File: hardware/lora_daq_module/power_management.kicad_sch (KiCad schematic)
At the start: 28 parts, among them J7 Conn_01x02, U6 MCP1700x-330xxTT, U7 TPS2116DRL, U8 TPS63002, U9 MCP73833

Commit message: assign parts and update BOM in symbol field table, warn: pcb footprints need update
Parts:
- C14: Desc (none) -> CAP CER 0.047UF 25V X7R 0603; Dist (none) -> Digikey; Dist PN (none) -> 311-1373-1-ND; Mfr (none) -> YAGEO; Mfr PN (none) -> CC0603KRX7R8BB473
- C15, C16, C17, C20, C21: Desc (none) -> CAP CER 1UF 16V X7R 0603; Dist (none) -> Digikey; Dist PN (none) -> 490-5241-1-ND; Mfr (none) -> Murata Electronics; Mfr PN (none) -> GCM188R71C105KA64D
- C18: Desc (none) -> CAP CER 10UF 50V X5R 1206; Dist (none) -> Digikey; Dist PN (none) -> 1276-2876-1-ND; Mfr (none) -> Samsung Electro-Mechanics; Mfr PN (none) -> CL31A106KBHNNNE
- C19: footprint Capacitor_SMD:C_1210_3225Metric -> Capacitor_SMD:C_1206_3216Metric; Desc (none) -> CAP CER 33UF 16V JB 1206; Dist (none) -> Digikey; Dist PN (none) -> 445-11694-1-ND; Mfr (none) -> TDK Corporation; Mfr PN (none) -> C3216JB1C336M160AB
- D4: value ~ -> Green; Desc (none) -> Green 571nm LED Indication - Discrete 2V 0603 (1608 Metric); Dist (none) -> Digikey; Dist PN (none) -> 160-1446-1-ND; Mfr (none) -> Lite-On Inc.; Mfr PN (none) -> LTST-C191KGKT
- D5: value ~ -> Yellow; Desc (none) -> Yellow 591nm LED Indication - Discrete 2.1V 0603 (1608 Metr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; Dist (none) -> Digikey; Dist PN (none) -> 160-1448-1-ND; Mfr (none) -> Lite-On Inc.; Mfr PN (none) -> LTST-C191KSKT
- D6: value ~ -> Red; Desc (none) -> Red 631nm LED Indication - Discrete 2V 0603 (1608 Metric); Dist (none) -> Digikey; Dist PN (none) -> 160-1436-1-ND; Mfr (none) -> Lite-On Inc.; Mfr PN (none) -> LTST-C190KRKT
- J7: Desc (none) -> Connector Header Through Hole 2 position 0.100" (2.54mm); Dist (none) -> Digikey; Dist PN (none) -> 732-5315-ND; Mfr (none) -> Würth Elektronik; Mfr PN (none) -> 61300211121
- L2: Desc (none) -> 3.3 µH Shielded Inductor 1.4 A 130mOhm Max Nonstandard; Dist (none) -> Digikey; Dist PN (none) -> 2457-LPS3015-332MRC-ND; Mfr (none) -> Coilcraft; Mfr PN (none) -> LPS3015-332MRC
- R10: Desc (none) -> 680 kOhms ±1% 0.1W, 1/10W Chip Resistor 0603 (1608 Metric) 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; Dist (none) -> Digikey; Dist PN (none) -> 311-680KHRCT-ND; Mfr (none) -> YAGEO; Mfr PN (none) -> RC0603FR-07680KL
- R11: Desc (none) -> 470 kOhms ±1% 0.1W, 1/10W Chip Resistor 0603 (1608 Metric) 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; Dist (none) -> Digikey; Dist PN (none) -> RMCF0603FT470KCT-ND; Mfr (none) -> Stackpole Electronics Inc; Mfr PN (none) -> RMCF0603FT470K
- R12: Desc (none) -> 4.7 kOhms ±5% 0.1W, 1/10W Chip Resistor 0603 (1608 Metric) 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; Dist (none) -> Digikey; Dist PN (none) -> 311-4.7KGRCT-ND; Mfr (none) -> YAGEO; Mfr PN (none) -> RC0603JR-074K7L
- R13, R14, R15: Desc (none) -> 470 Ohms ±5% 0.1W, 1/10W Chip Resistor 0603 (1608 Metric) M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; Dist (none) -> Digikey; Dist PN (none) -> 311-470GRCT-ND; Mfr (none) -> YAGEO; Mfr PN (none) -> RC0603JR-07470RL
- R16, R19: Desc (none) -> 1 kOhms ±1% 0.1W, 1/10W Chip Resistor 0603 (1608 Metric) Au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; Dist (none) -> Digikey; Dist PN (none) -> RMCF0603FT1K00CT-ND; Mfr (none) -> Stackpole Electronics Inc; Mfr PN (none) -> RMCF0603FT1K00
- R17: Desc (none) -> THERMISTOR NTC 10KOHM 3380K 0603; Dist (none) -> Digikey; Dist PN (none) -> 490-16279-1-ND; Mfr (none) -> Murata Electronics; Mfr PN (none) -> NCU18XH103F60RB
- R18: Desc (none) -> 150 kOhms ±1% 0.1W, 1/10W Chip Resistor 0603 (1608 Metric) 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; Dist (none) -> Digikey; Dist PN (none) -> RMCF0603FT150KCT-ND; Mfr (none) -> Stackpole Electronics Inc; Mfr PN (none) -> RMCF0603FT150K
- U6: Desc (none) -> Linear Voltage Regulator IC Positive Fixed 1 Output 250mA S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; Dist (none) -> Digikey; Dist PN (none) -> MCP1700T3302ETTCT-ND; Mfr (none) -> Microchip Technology; Mfr PN (none) -> MCP1700T-3302E/TT
- U7: Desc (none) -> Power Switch/Driver 2:1 N-Channel 2.5A SOT-583; Dist (none) -> Digikey; Dist PN (none) -> 296-TPS2116DRLRCT-ND; Mfr (none) -> Texas Instruments; Mfr PN (none) -> TPS2116DRLR
- U8: Desc (none) -> Buck-Boost Switching Regulator IC Positive Fixed 5V 1 Outpu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; Dist (none) -> Digikey; Dist PN (none) -> 296-19644-1-ND; Mfr (none) -> Texas Instruments; Mfr PN (none) -> TPS63002DRCR
- U9: Desc (none) -> Charger IC Lithium Ion/Polymer 10-MSOP; Dist (none) -> Digikey; Dist PN (none) -> MCP73833T-AMI/UNCT-ND; Mfr (none) -> Microchip Technology; Mfr PN (none) -> MCP73833T-AMI/UN

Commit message: add test points and antenna microstrip
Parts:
- added TP13: tp_batgnd, TestPoint:TestPoint_THTPad_1.5x1.5mm_Drill0.7mm, symbol Connector:TestPoint
- added TP2: tp_vbatt, TestPoint:TestPoint_THTPad_1.5x1.5mm_Drill0.7mm, symbol Connector:TestPoint
- added TP3: tp_5vbatt, TestPoint:TestPoint_THTPad_1.5x1.5mm_Drill0.7mm, symbol Connector:TestPoint
- added TP4: tp_5v, TestPoint:TestPoint_THTPad_1.5x1.5mm_Drill0.7mm, symbol Connector:TestPoint
- added TP5: tp_3v3, TestPoint:TestPoint_THTPad_1.5x1.5mm_Drill0.7mm, symbol Connector:TestPoint
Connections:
- net +3.3V: now also TP5.1
- net +5V: now also TP4.1
- net +5V_bat: now also TP3.1
- net +VBATT: now also TP2.1
- net GND: now also TP13.1

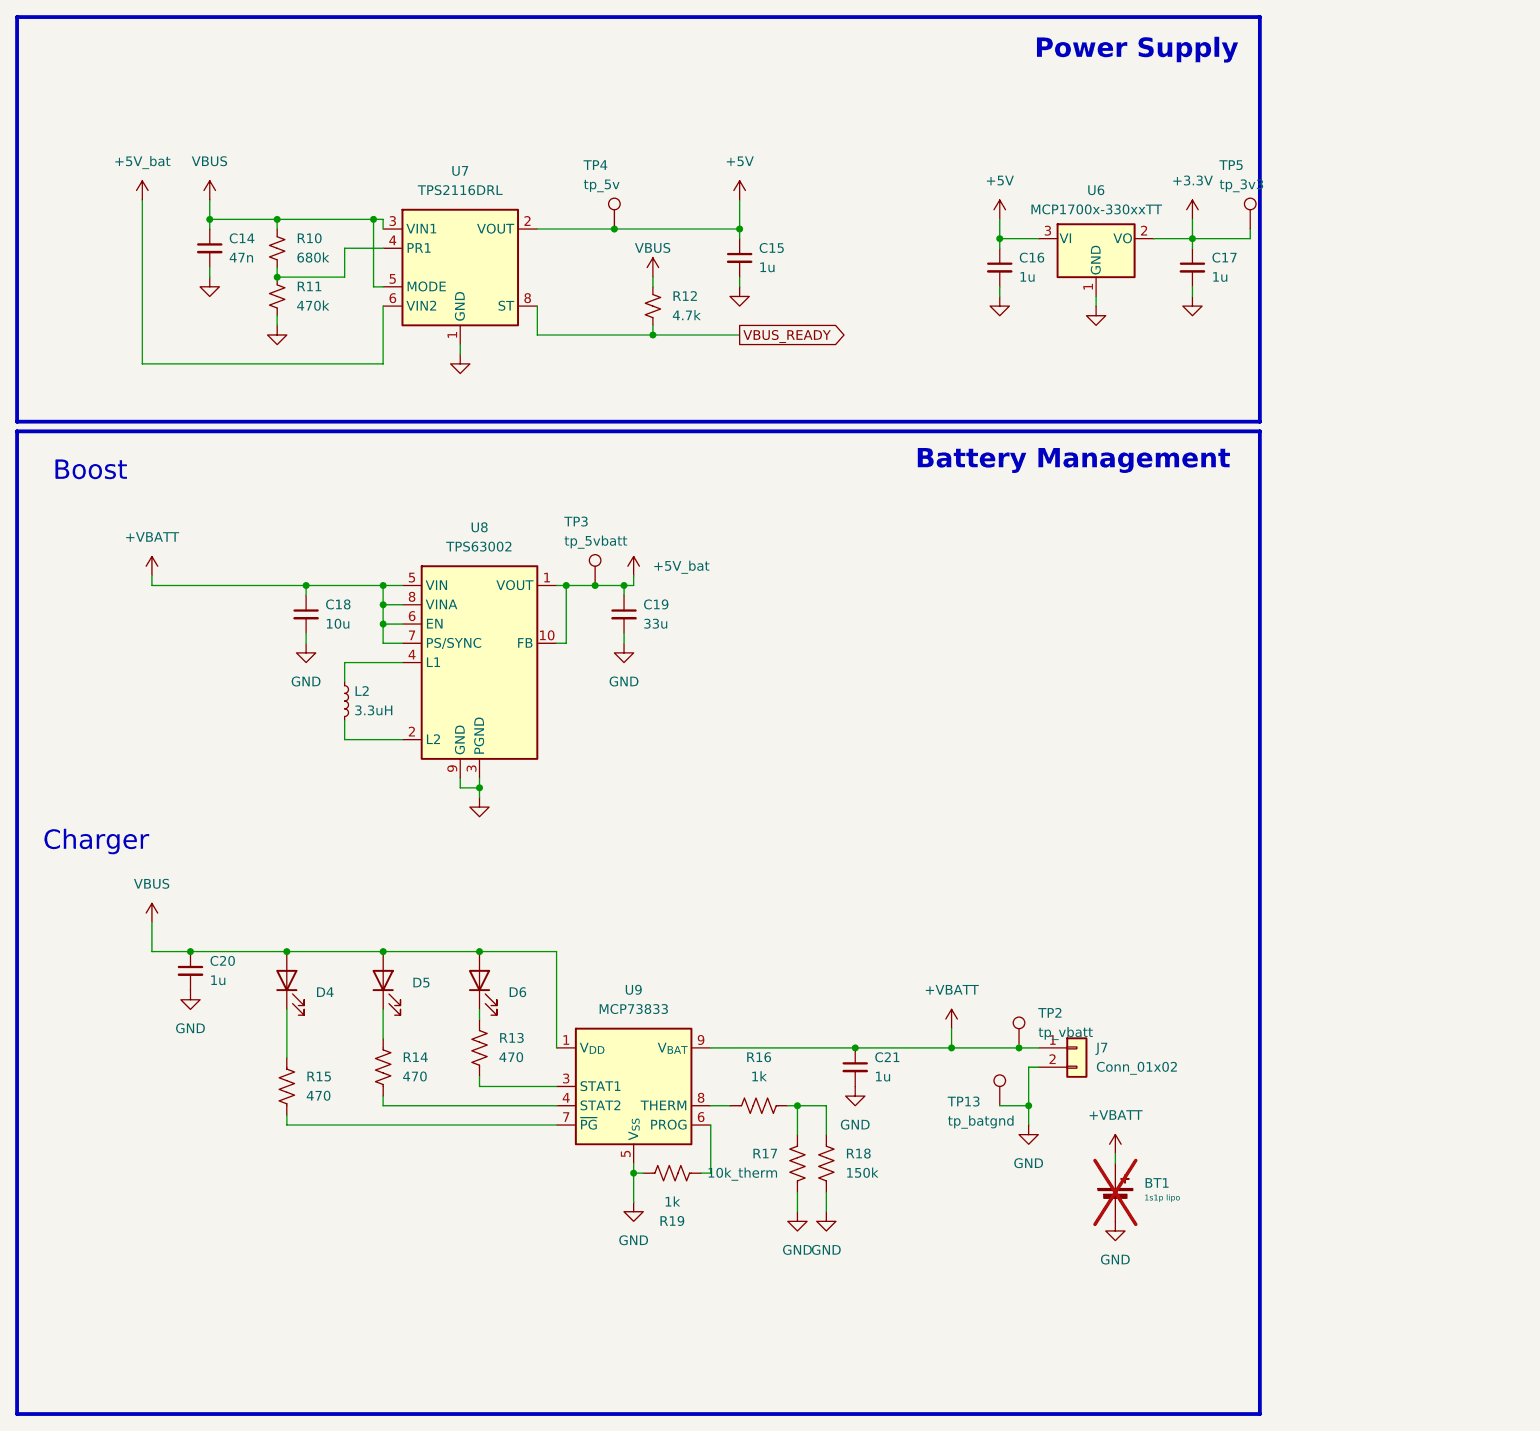
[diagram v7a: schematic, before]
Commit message: add ohm resistors for power schematic, update design rules for jlc
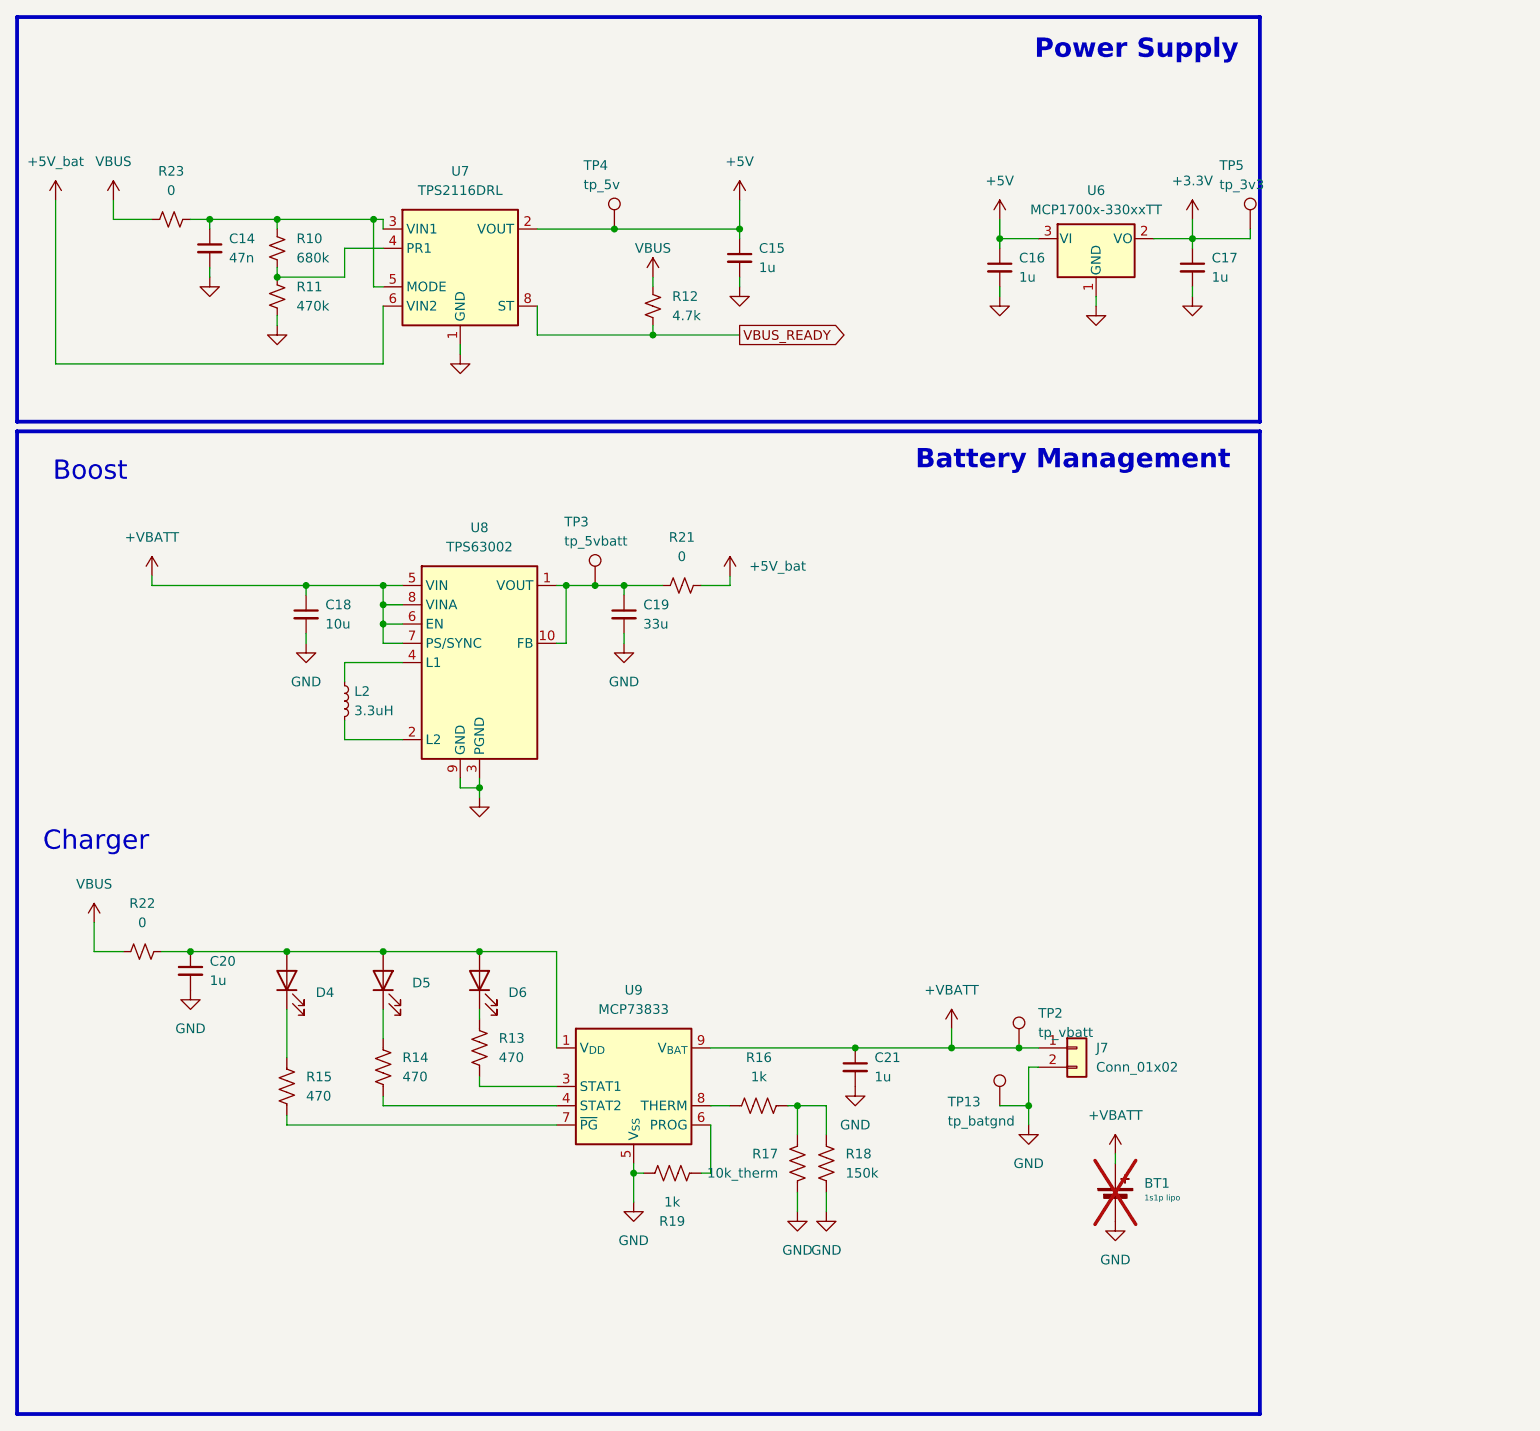
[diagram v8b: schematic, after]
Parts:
- added R21, R22, R23: 0, Resistor_SMD:R_1812_4532Metric, symbol Device:R_Small_US
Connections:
- net +5V_bat: now also R21.2; no longer C19.1, TP3.1, U8.1 (VOUT), U8.10 (FB)
- net VBUS: now also R22.1, R23.1; no longer C14.1, C20.1, D4.2 (A), D5.2 (A), D6.2 (A), R10.1, U7.3 (VIN1), U7.5 (MODE), U9.1 (V_{DD}), U9.2 (V_{DD})
- new net: C19.1, R21.1, TP3.1, U8.1 (VOUT), U8.10 (FB)
- new net: C20.1, D4.2 (A), D5.2 (A), D6.2 (A), R22.2, U9.1 (V_{DD}), U9.2 (V_{DD})
- new net: C14.1, R10.1, R23.2, U7.3 (VIN1), U7.5 (MODE)
